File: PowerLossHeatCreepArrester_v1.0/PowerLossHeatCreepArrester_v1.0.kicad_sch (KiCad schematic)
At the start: 58 parts, among them J1 Conn_01x04_Socket, J2 BC3550Y0302A, J3 Conn_01x04_Pin, Q1 BSS138, Q2 BSS138, U1 LM393, U2 MT3608, U3 TP4056-42-ESOP8, U5 MP1584EN

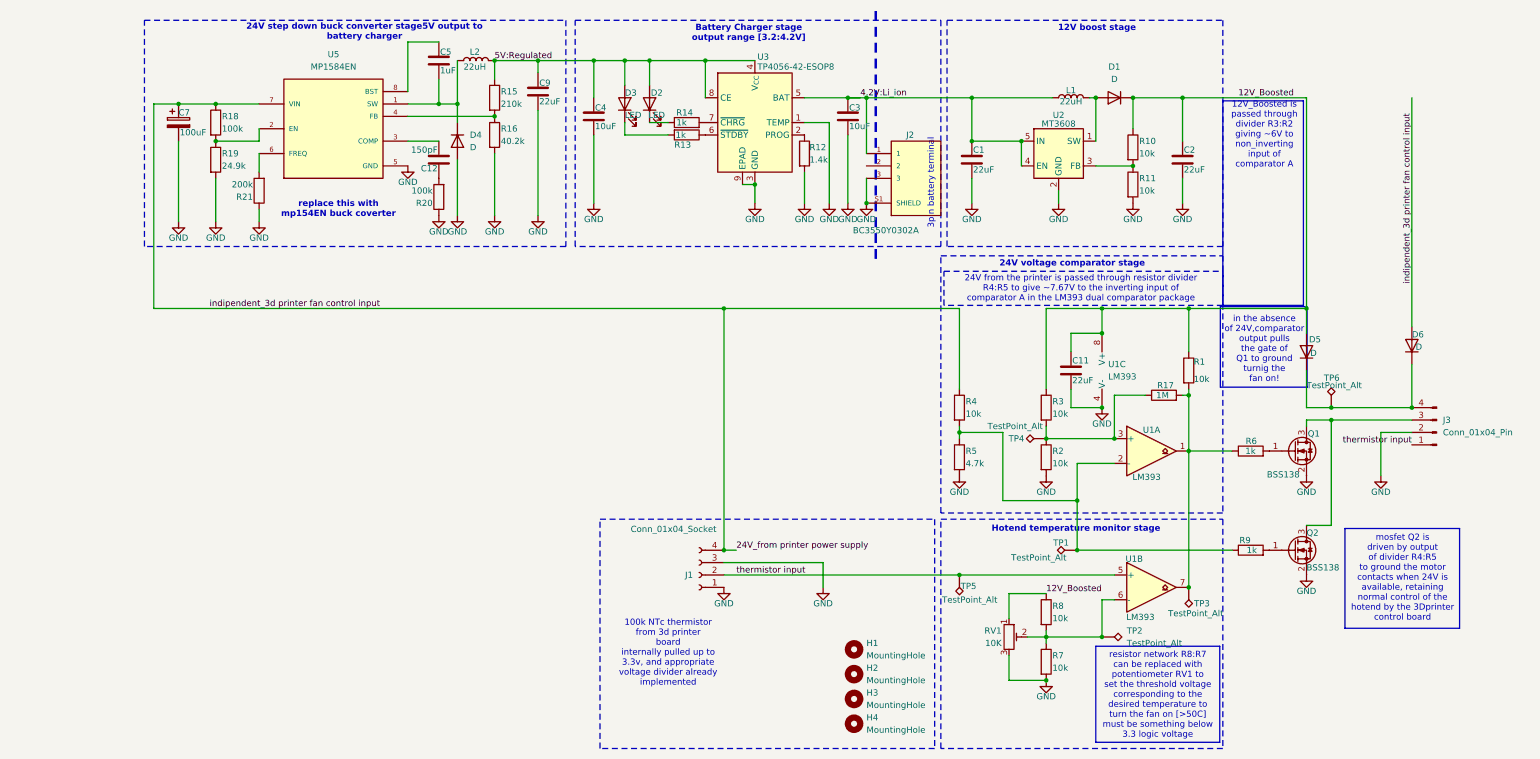
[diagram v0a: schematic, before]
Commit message: rev_1.0: independent temperature sensing, comparator divider redesign
Hardware changes:
- Add U4: independent temperature monitoring IC with dedicated thermistor.
  Sharing the printer's NTC directly with this board is not feasible without
  a 3.3 V interface solution; U4 provides an isolated temperature signal to
  LM393 comparator 2 for the > 50 °C fan activation threshold.

Schematic (kicad_sch):
- Recalculate comparator 1 (power-loss) voltage divider:
    R15: 210k → 52.3k
    R16: 40.2k → 10k
- Update hysteresis / reference network:
    R21: 200k → 100k
    Comparator reference resistors: 10k → 47k and 10k → 910k
- Reroute GND symbol and reposition thermistor net label for clarity
- Add schematic note documenting the thermistor isolation decision
- Fix net label typo: 'indipendent' → 'independent'
- Minor wording update in annotation text (package → chip)

PCB layout (kicad_pcb):
- Place U4 footprint at (138.51, 88.06, 90°) on F.Cu
- Update net assignments on affected pads to match schematic
- Set solder_mask_to_copper_clearance: 0.0 → 0.005 mm
- Add back-silkscreen label and minor component placement adjustments

Project file (kicad_pro):
- Record U4 in used_designators
- Persist updated DRC constraint (solder mask clearance 0.005 mm)

Documentation (README.md):
- Add Independent temperature monitoring row to Design Notes table
- Add Revision History section summarising rev_1.0 changes

Co-authored-by: Copilot <223556219+Copilot@users.noreply.github.com>
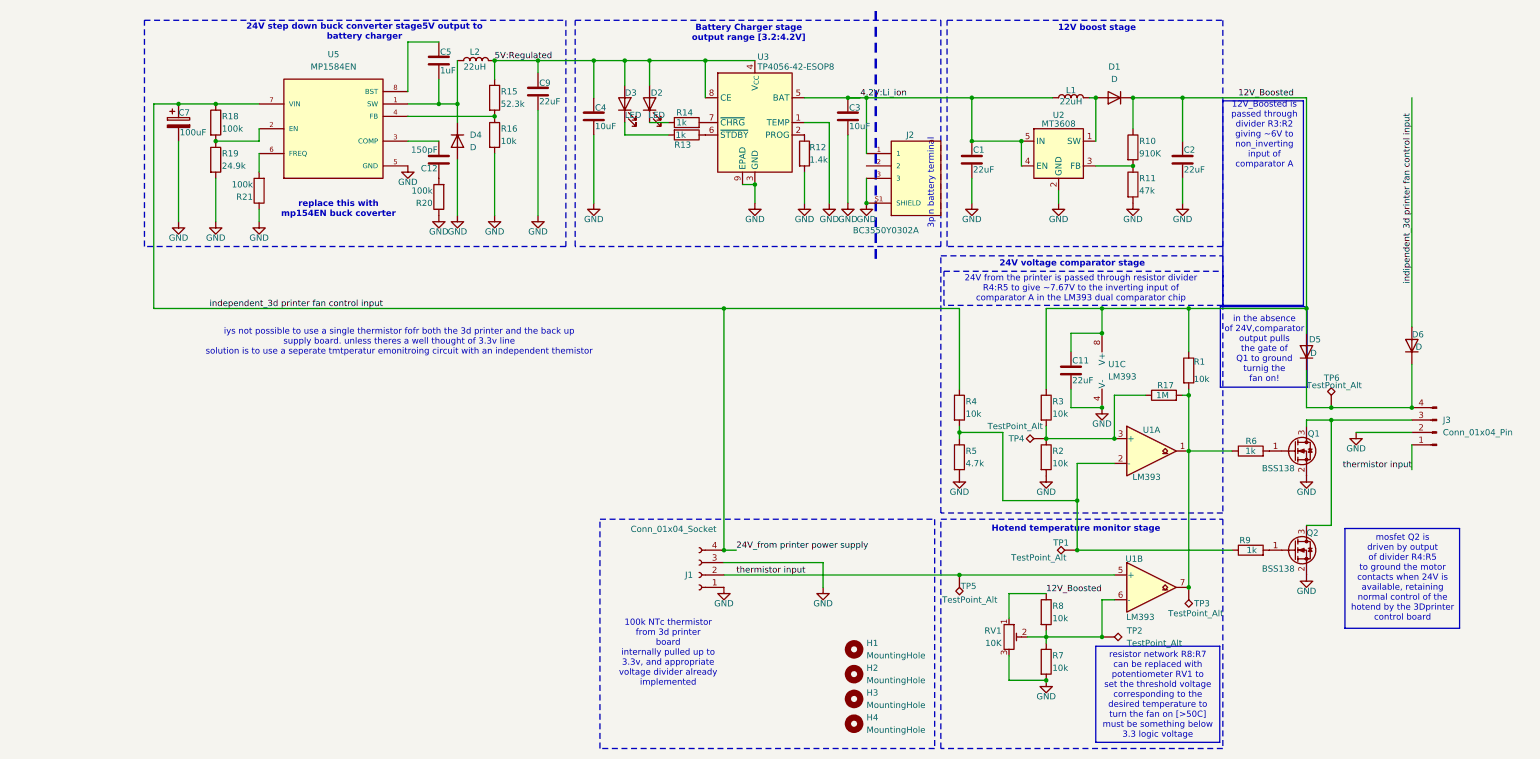
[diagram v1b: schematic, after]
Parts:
- R10: value 10k -> 910K
- R11: value 10k -> 47k
- R15: value 210k -> 52.3k
- R16: value 40.2k -> 10k
- R21: value 200k -> 100k
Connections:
- net 24V_from printer power supply: no longer D6.2 (A)
- new net indipendent_3d printer fan control input: D6.2 (A)
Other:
- note added: "24V from the printer is passed through resistor divider R4:R5 to give ~7.67V to the inverting input of comparator A in the LM393 dual comparator chip"
- note added: "iys not possible to use a single thermistor fofr both the 3d printer and the back up supply board. unless theres a well thought of 3.3v line solution is to use a seperate tmtperatur emonitroing circuit with an independent themistor"
- note removed: "24V from the printer is passed through resistor divider R4:R5 to give ~7.67V to the inverting input of comparator A in the LM393 dual comparator package"
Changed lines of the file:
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@@
 		)
 	)
-	(text "\n24V from the printer is passed through resistor divider \nR4:R5 to give ~7.67V to the inverting input of  \ncomparator A in the LM393 dual comparator package"
+	(text "\n24V from the printer is passed through resistor divider \nR4:R5 to give ~7.67V to the inverting input of  \ncomparator A in the LM393 dual comparator chip"
 		(exclude_from_sim no)
 		(at 205.232 67.31 0)
@@
 		)
 	)
+	(text "iys not possible to use a single thermistor fofr both the 3d printer and the back up\nsupply board. unless theres a well thought of 3.3v line \nsolution is to use a seperate tmtperatur emonitroing circuit with an independent themistor\n"
+		(exclude_from_sim no)
+		(at 65.532 79.248 0)
+		(effects
+			(font
+				(size 1.27 1.27)
+			)
+		)
+	)
 	(text "3pin battery terminal\n"
 		(exclude_from_sim no)
@@
 	(wire
 		(pts
-			(xy 266.7 97.79) (xy 273.05 97.79)
+			(xy 261.62 97.79) (xy 273.05 97.79)
 		)
 		(stroke
@@
 	(wire
 		(pts
-			(xy 266.7 106.68) (xy 266.7 97.79)
-		)
-		(stroke
-			(width 0)
-			(type default)
-		)
-	)
-	(wire
-		(pts
 			(xy 193.04 38.1) (xy 193.04 43.18)
 		)
@@
 	(wire
 		(pts
+			(xy 273.05 105.41) (xy 273.05 100.33)
+		)
+		(stroke
+			(width 0)
+			(type default)
+		)
+	)
+	(wire
+		(pts
 			(xy 132.08 127) (xy 180.34 127)
 		)
@@
 	)
 	(label "thermistor input"
-		(at 273.05 100.33 180)
+		(at 273.05 105.41 180)
 		(effects
 			(font
@@
 		)
 	)
-	(label "indipendent_3d printer fan control input"
+	(label "independent_3d printer fan control input"
 		(at 26.67 72.39 0)
 		(effects
@@
 	(symbol
 		(lib_id "power:GND")
-		(at 266.7 106.68 0)
+		(at 261.62 97.79 0)
 		(unit 1)
 		(body_style 1)
@@
 		(dnp no)
 		(property "Reference" "#PWR020"
-			(at 266.7 113.03 0)
+			(at 261.62 104.14 0)
 			(hide yes)
 			(show_name no)
@@
 		)
 		(property "Value" "GND"
-			(at 266.7 109.982 0)
+			(at 261.62 101.092 0)
 			(show_name no)
 			(do_not_autoplace no)
@@
 		)
 		(property "Footprint" ""
-			(at 266.7 106.68 0)
+			(at 261.62 97.79 0)
 			(hide yes)
 			(show_name no)
@@
 		)
 		(property "Datasheet" ""
-			(at 266.7 106.68 0)
+			(at 261.62 97.79 0)
 			(hide yes)
 			(show_name no)
@@
 		)
 		(property "Description" "Power symbol creates a global label with name \"GND\" , ground"
-			(at 266.7 106.68 0)
+			(at 261.62 97.79 0)
 			(hide yes)
 			(show_name no)
@@
 		)
 		(property "Value" "BSS138"
-			(at 243.332 106.426 0)
+			(at 242.316 105.156 0)
 			(show_name no)
 			(do_not_autoplace no)
@@
 			)
 		)
-		(property "Value" "10k"
+		(property "Value" "47k"
 			(at 217.17 48.26 0)
 			(show_name no)
@@
 			)
 		)
-		(property "Value" "210k"
+		(property "Value" "52.3k"
 			(at 86.36 30.48 0)
 			(show_name no)
@@
 		)
 		(property "Value" "BSS138"
-			(at 251.46 125.476 0)
+			(at 242.316 125.73 0)
 			(show_name no)
 			(do_not_autoplace no)
@@
 			)
 		)
-		(property "Value" "40.2k"
+		(property "Value" "10k"
 			(at 86.36 38.1 0)
 			(show_name no)
@@
 			)
 		)
-		(property "Value" "200k"
+		(property "Value" "100k"
 			(at 35.56 46.99 0)
 			(show_name no)
@@
 			)
 		)
-		(property "Value" "10k"
+		(property "Value" "910K"
 			(at 217.17 40.64 0)
 			(show_name no)

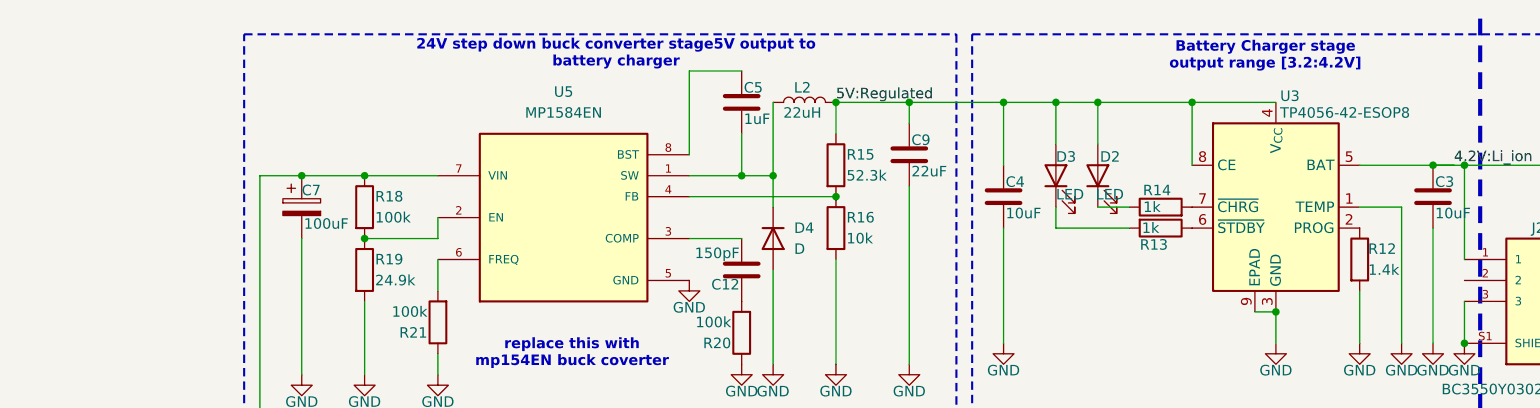
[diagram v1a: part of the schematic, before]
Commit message: Schematic: add reverse polarity protection design notes
- 24V input side: ZXMP6A13FTA P-ch SOT-23 recommended
  (Source=24V_IN, Drain=rail, Gate=GND via 10k; Vgs=-24V fully enhanced,
  Rds<400mohm, ~100mW dissipation at 0.5A)
- Battery side: AO3401A recommended over ZXMP6A13FTA
  (ZXMP6A13FTA unsuitable: Vgs=-3.7V gives ~900mohm Rds, exceeds 1.1A Id
  limit at fan loads >130mA; AO3401A same SOT-23 footprint, 50mohm, Id=4A)

Co-authored-by: Copilot <223556219+Copilot@users.noreply.github.com>
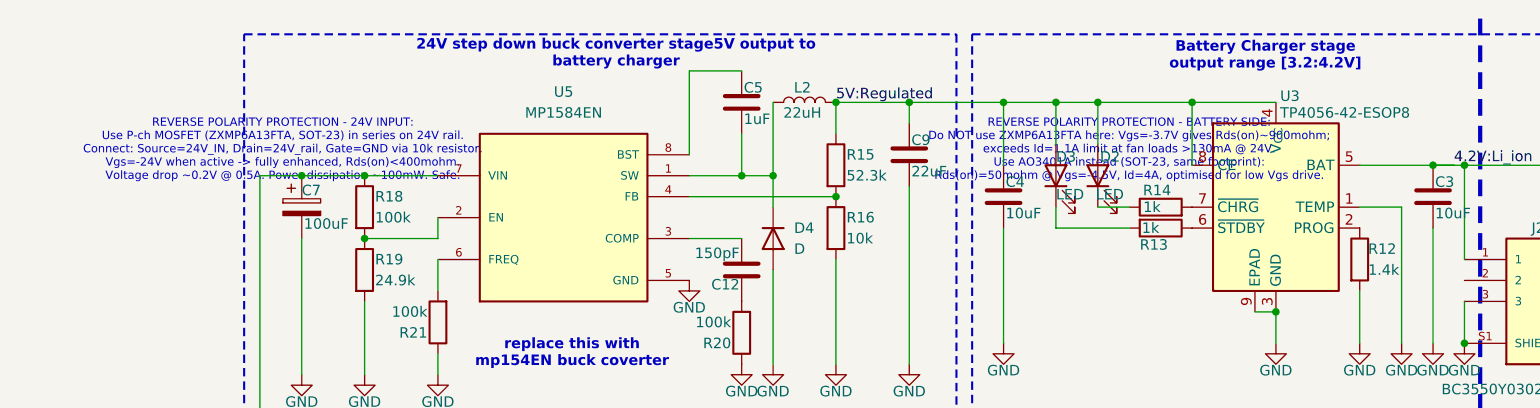
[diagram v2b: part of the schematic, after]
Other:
- note added: "REVERSE POLARITY PROTECTION - 24V INPUT: Use P-ch MOSFET (ZXMP6A13FTA, SOT-23) in series on 24V rail. Connect: Source=24V_IN, Drain=24V_rail, Gate=GND via 10k resistor. Vgs=-24V when active -> fully enhanced, Rds(on)<400mohm. Voltage drop ~0.2V @ 0.5A. Power dissipation ~100mW. Safe."
- note added: "REVERSE POLARITY PROTECTION - BATTERY SIDE: Do NOT use ZXMP6A13FTA here: Vgs=-3.7V gives Rds(on)~900mohm; exceeds Id=1.1A limit at fan loads >130mA @ 24V. Use AO3401A instead (SOT-23, same footprint): Rds(on)=50mohm @ Vgs=-4.5V, Id=4A, optimised for low Vgs drive."
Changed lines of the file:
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@@
+		)
+	)
+	(text "REVERSE POLARITY PROTECTION - 24V INPUT:\nUse P-ch MOSFET (ZXMP6A13FTA, SOT-23) in series on 24V rail.\nConnect: Source=24V_IN, Drain=24V_rail, Gate=GND via 10k resistor.\nVgs=-24V when active -> fully enhanced, Rds(on)<400mohm.\nVoltage drop ~0.2V @ 0.5A. Power dissipation ~100mW. Safe."
+		(exclude_from_sim no)
+		(at 18.034 27.432 0)
+		(effects
+			(font
+				(size 1.0 1.0)
+				(color 0 0 128 1)
+			)
+		)
+	)
+	(text "REVERSE POLARITY PROTECTION - BATTERY SIDE:\nDo NOT use ZXMP6A13FTA here: Vgs=-3.7V gives Rds(on)~900mohm;\nexceeds Id=1.1A limit at fan loads >130mA @ 24V.\nUse AO3401A instead (SOT-23, same footprint):\nRds(on)=50mohm @ Vgs=-4.5V, Id=4A, optimised for low Vgs drive."
+		(exclude_from_sim no)
+		(at 120.65 27.432 0)
+		(effects
+			(font
+				(size 1.0 1.0)
+				(color 128 0 0 1)
+			)
 		)
 	)

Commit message: rev_1.0: add Q3 reverse protection on fan control input
- Q3 (ZXMP6A13FTA, SOT-23, P-ch): placed on 'independent_3d printer
  fan control input' net at (22.86, 88.9)
  Source = fan control rail, Drain = protected node, Gate = GND via R23
- R23 (10k, 0603): gate pull-down resistor for Q3
  Vgs = -(rail voltage) when correct polarity -> MOSFET fully on
  Reversed polarity -> Vgs = 0 -> MOSFET off, circuit protected
  ZXMP6A13FTA suitable here: signal/control line, negligible current
- Schematic note retained: 24V input and battery side protection
  still to be implemented (ZXMP6A13FTA for 24V, AO3401A for battery)
- PCB layout and project file updated to match

Co-authored-by: Copilot <223556219+Copilot@users.noreply.github.com>
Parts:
- added 5V1, GND1: TestPoint_Alt, TestPoint:TestPoint_Pad_D1.5mm, symbol Connector:TestPoint_Alt
- added Q3: ZXMP6A13FTA, SMD-MOSFET-P-CH-60V-900MA-ZXMP6A13FTA_SOT-23_:SOT-23, symbol SMD-MOSFET-P-CH-60V-900MA-ZXMP6A13FTA_SOT-23_:SMD-MOSFET-P-CH-60V-900MA-ZXMP6A1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
- added R22: 100k, Resistor_SMD:R_0603_1608Metric, symbol Device:R
- added R23: 10k, Resistor_SMD:R_0603_1608Metric, symbol Device:R
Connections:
- net 12V_Boosted: now also J1.1 (Pin_1)
- net 24V_from printer power supply: now also Q3.3
- net 5V:Regulated: now also 5V1.1
- net GND: now also GND1.1, R22.2, R23.1; no longer J1.1 (Pin_1)
- net thermistor input: now also R22.1
- new net: Q3.1, R23.2
- new net independent_3d printer fan control input: Q3.2
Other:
- note added: "add reverse protection on the power input side, as well ass the battery side"
- note removed: "REVERSE POLARITY PROTECTION - 24V INPUT: Use P-ch MOSFET (ZXMP6A13FTA, SOT-23) in series on 24V rail. Connect: Source=24V_IN, Drain=24V_rail, Gate=GND via 10k resistor. Vgs=-24V when active -> fully enhanced, Rds(on)<400mohm. Voltage drop ~0.2V @ 0.5A. Power dissipation ~100mW. Safe."
- note removed: "REVERSE POLARITY PROTECTION - BATTERY SIDE: Do NOT use ZXMP6A13FTA here: Vgs=-3.7V gives Rds(on)~900mohm; exceeds Id=1.1A limit at fan loads >130mA @ 24V. Use AO3401A instead (SOT-23, same footprint): Rds(on)=50mohm @ Vgs=-4.5V, Id=4A, optimised for low Vgs drive."
- note removed: "replace this with mp154EN buck coverter"
